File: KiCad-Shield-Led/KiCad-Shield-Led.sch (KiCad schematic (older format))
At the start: 8 parts, among them P1 Power, P2 Analog, P3 Digital, P4 Digital, P5 CONN_01X01, P6 CONN_01X01, P7 CONN_01X01, P8 CONN_01X01

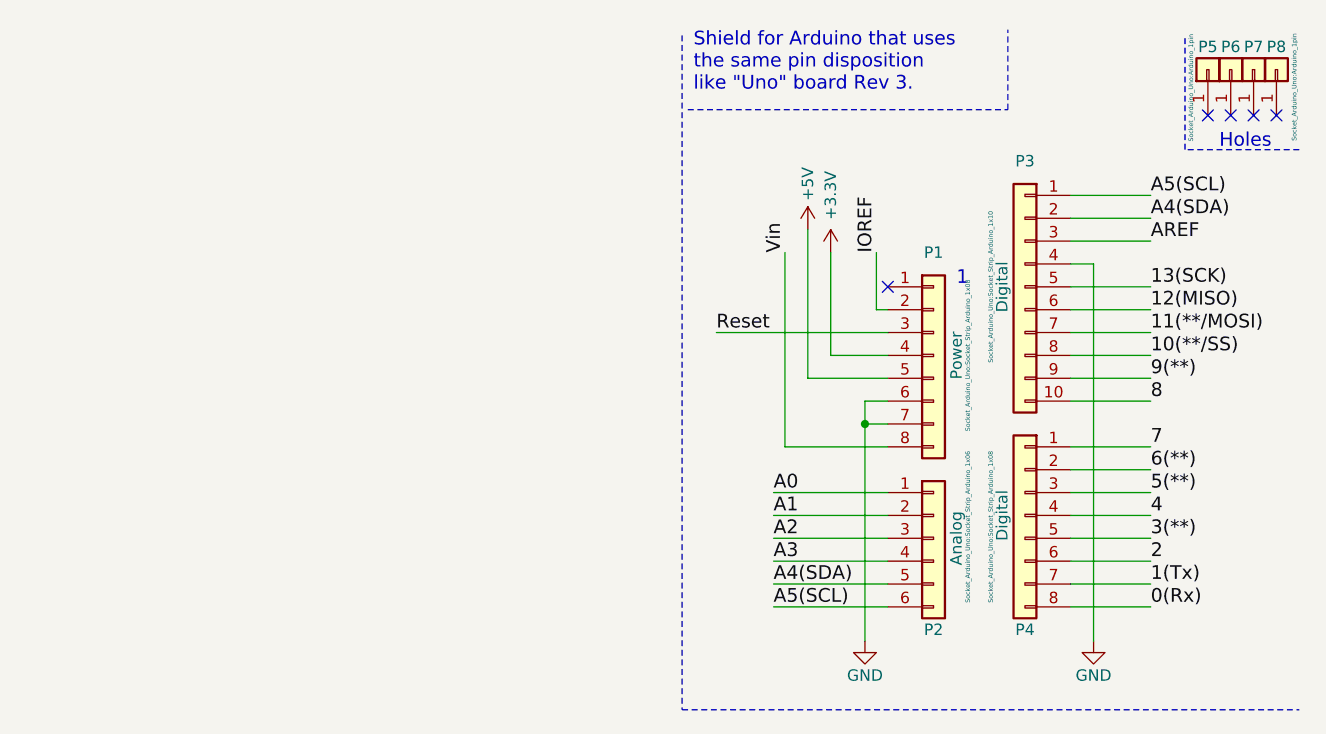
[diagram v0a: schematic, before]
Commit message: Dessin LED et R
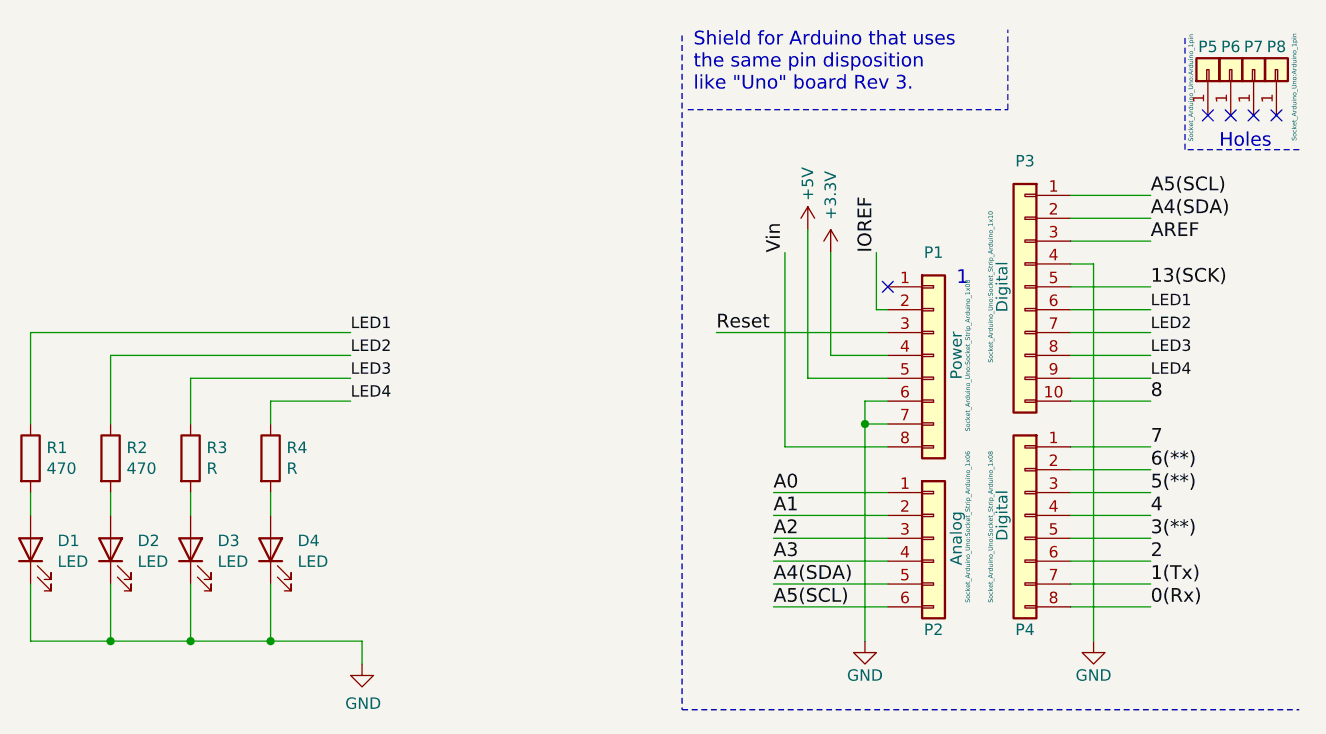
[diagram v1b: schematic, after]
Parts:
- added D1, D2, D3, D4: LED, symbol Device:LED
- added R1, R2: 470, symbol Device:R
- added R3, R4: R, symbol Device:R
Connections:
- net GND: now also D1.1 (K), D2.1 (K), D3.1 (K), D4.1 (K)
- net 10(**/SS) renamed LED3
- net LED3: now also R3.1
- net 11(**/MOSI) renamed LED2
- net LED2: now also R2.1
- net 12(MISO) renamed LED1
- net LED1: now also R1.1
- net 9(**) renamed LED4
- net LED4: now also R4.1
- new net: D1.2 (A), R1.2
- new net: D2.2 (A), R2.2
- new net: D3.2 (A), R3.2
- new net: D4.2 (A), R4.2
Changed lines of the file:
@@
 Text Label 10550 2100 0    60   ~ 0
 8
-Text Label 10550 2000 0    60   ~ 0
-9(**)
-Text Label 10550 1900 0    60   ~ 0
-10(**/SS)
-Text Label 10550 1800 0    60   ~ 0
-11(**/MOSI)
-Text Label 10550 1700 0    60   ~ 0
-12(MISO)
 Text Label 10550 1600 0    60   ~ 0
 13(SCK)
@@
 Wire Notes Line
 	10700 1000 10700 500
+$Comp
+L Device:LED D1
+U 1 1 5FC4CFF8
+P 5650 2750
+F 0 "D1" V 5689 2632 50  0000 R CNN
+F 1 "LED" V 5598 2632 50  0000 R CNN
+F 2 "" H 5650 2750 50  0001 C CNN
+F 3 "~" H 5650 2750 50  0001 C CNN
+	1    5650 2750
+	0    -1   -1   0
+$EndComp
+$Comp
+L Device:R R1
+U 1 1 5FC4E899
+P 5650 2350
+F 0 "R1" H 5720 2396 50  0000 L CNN
+F 1 "470" H 5720 2305 50  0000 L CNN
+F 2 "" V 5580 2350 50  0001 C CNN
+F 3 "~" H 5650 2350 50  0001 C CNN
+	1    5650 2350
+	1    0    0    -1
+$EndComp
+Wire Wire Line
+	5650 2500 5650 2600
+Wire Wire Line
+	5650 2900 5650 3150
+Wire Wire Line
+	5650 3150 6000 3150
+Wire Wire Line
+	7100 3150 7100 3250
+$Comp
+L Device:LED D2
+U 1 1 5FC5721B
+P 6000 2750
+F 0 "D2" V 6039 2632 50  0000 R CNN
+F 1 "LED" V 5948 2632 50  0000 R CNN
+F 2 "" H 6000 2750 50  0001 C CNN
+F 3 "~" H 6000 2750 50  0001 C CNN
+	1    6000 2750
+	0    -1   -1   0
+$EndComp
+$Comp
+L Device:R R2
+U 1 1 5FC5738B
+P 6000 2350
+F 0 "R2" H 6070 2396 50  0000 L CNN
+F 1 "470" H 6070 2305 50  0000 L CNN
+F 2 "" V 5930 2350 50  0001 C CNN
+F 3 "~" H 6000 2350 50  0001 C CNN
+	1    6000 2350
+	1    0    0    -1
+$EndComp
+Wire Wire Line
+	6000 2500 6000 2600
+Wire Wire Line
+	6000 2900 6000 3150
+Connection ~ 6000 3150
+Wire Wire Line
+	6000 3150 6350 3150
+$Comp
+L Device:LED D3
+U 1 1 5FC5A1AB
+P 6350 2750
+F 0 "D3" V 6389 2632 50  0000 R CNN
+F 1 "LED" V 6298 2632 50  0000 R CNN
+F 2 "" H 6350 2750 50  0001 C CNN
+F 3 "~" H 6350 2750 50  0001 C CNN
+	1    6350 2750
+	0    -1   -1   0
+$EndComp
+$Comp
+L Device:R R3
+U 1 1 5FC5A343
+P 6350 2350
+F 0 "R3" H 6420 2396 50  0000 L CNN
+F 1 "R" H 6420 2305 50  0000 L CNN
+F 2 "" V 6280 2350 50  0001 C CNN
+F 3 "~" H 6350 2350 50  0001 C CNN
+	1    6350 2350
+	1    0    0    -1
+$EndComp
+Wire Wire Line
+	6350 2500 6350 2600
+Wire Wire Line
+	6350 2900 6350 3150
+$Comp
+L Device:LED D4
+U 1 1 5FC5A34F
+P 6700 2750
+F 0 "D4" V 6739 2632 50  0000 R CNN
+F 1 "LED" V 6648 2632 50  0000 R CNN
+F 2 "" H 6700 2750 50  0001 C CNN
+F 3 "~" H 6700 2750 50  0001 C CNN
+	1    6700 2750
+	0    -1   -1   0
+$EndComp
+$Comp
+L Device:R R4
+U 1 1 5FC5A359
+P 6700 2350
+F 0 "R4" H 6770 2396 50  0000 L CNN
+F 1 "R" H 6770 2305 50  0000 L CNN
+F 2 "" V 6630 2350 50  0001 C CNN
+F 3 "~" H 6700 2350 50  0001 C CNN
+	1    6700 2350
+	1    0    0    -1
+$EndComp
+Wire Wire Line
+	6700 2500 6700 2600
+Wire Wire Line
+	6700 2900 6700 3150
+Connection ~ 6350 3150
+Wire Wire Line
+	6350 3150 6700 3150
+Connection ~ 6700 3150
+Wire Wire Line
+	6700 3150 7100 3150
+$Comp
+L power:GND #PWR05
+U 1 1 5FC5CA17
+P 7100 3250
+F 0 "#PWR05" H 7100 3000 50  0001 C CNN
+F 1 "GND" H 7105 3077 50  0000 C CNN
+F 2 "" H 7100 3250 50  0001 C CNN
+F 3 "" H 7100 3250 50  0001 C CNN
+	1    7100 3250
+	1    0    0    -1
+$EndComp
+Wire Wire Line
+	6700 2200 6700 2100
+Wire Wire Line
+	6700 2100 7050 2100
+Wire Wire Line
+	6350 2200 6350 2000
+Wire Wire Line
+	6350 2000 7050 2000
+Wire Wire Line
+	6000 1900 7050 1900
+Wire Wire Line
+	6000 1900 6000 2200
+Wire Wire Line
+	5650 2200 5650 1800
+Wire Wire Line
+	5650 1800 7050 1800
+Text Label 7050 1800 0    50   ~ 0
+LED1
+Text Label 7050 1900 0    50   ~ 0
+LED2
+Text Label 7050 2000 0    50   ~ 0
+LED3
+Text Label 7050 2100 0    50   ~ 0
+LED4
+Text Label 10550 1700 0    50   ~ 0
+LED1
+Text Label 10550 1800 0    50   ~ 0
+LED2
+Text Label 10550 1900 0    50   ~ 0
+LED3
+Text Label 10550 2000 0    50   ~ 0
+LED4
 $EndSCHEMATC

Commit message: Fin du shematique
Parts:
- R3, R4: value R -> 470
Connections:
- no-connect marks 5 -> 23
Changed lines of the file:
@@
 P 6350 2350
 F 0 "R3" H 6420 2396 50  0000 L CNN
-F 1 "R" H 6420 2305 50  0000 L CNN
+F 1 "470" H 6420 2305 50  0000 L CNN
 F 2 "" V 6280 2350 50  0001 C CNN
 F 3 "~" H 6350 2350 50  0001 C CNN
@@
 P 6700 2350
 F 0 "R4" H 6770 2396 50  0000 L CNN
-F 1 "R" H 6770 2305 50  0000 L CNN
+F 1 "470" H 6770 2305 50  0000 L CNN
 F 2 "" V 6630 2350 50  0001 C CNN
 F 3 "~" H 6700 2350 50  0001 C CNN
@@
 Text Label 10550 2000 0    50   ~ 0
 LED4
+NoConn ~ 8900 2500
+NoConn ~ 8900 2600
+NoConn ~ 8900 2700
+NoConn ~ 8900 2800
+NoConn ~ 10550 2300
+NoConn ~ 10550 2400
+NoConn ~ 10550 2500
+NoConn ~ 10550 2600
+NoConn ~ 10550 2700
+NoConn ~ 10550 2800
+NoConn ~ 10550 2900
+NoConn ~ 10550 3000
+NoConn ~ 10550 2100
+NoConn ~ 10550 1600
+NoConn ~ 10550 1400
+NoConn ~ 8950 1450
+NoConn ~ 9350 1450
+NoConn ~ 8650 1800
+$Comp
+L power:PWR_FLAG #FLG0101
+U 1 1 5FC89307
+P 7150 850
+F 0 "#FLG0101" H 7150 925 50  0001 C CNN
+F 1 "PWR_FLAG" H 7150 1023 50  0000 C CNN
+F 2 "" H 7150 850 50  0001 C CNN
+F 3 "~" H 7150 850 50  0001 C CNN
+	1    7150 850
+	1    0    0    -1
+$EndComp
+$Comp
+L power:GND #PWR0101
+U 1 1 5FC89CAC
+P 7150 850
+F 0 "#PWR0101" H 7150 600 50  0001 C CNN
+F 1 "GND" H 7150 700 50  0000 C CNN
+F 2 "" H 7150 850 50  0000 C CNN
+F 3 "" H 7150 850 50  0000 C CNN
+	1    7150 850
+	1    0    0    -1
+$EndComp
+$Comp
+L power:+3.3V #PWR0102
+U 1 1 5FC8AE1D
+P 7600 850
+F 0 "#PWR0102" H 7600 700 50  0001 C CNN
+F 1 "+3.3V" V 7600 1100 50  0000 C CNN
+F 2 "" H 7600 850 50  0000 C CNN
+F 3 "" H 7600 850 50  0000 C CNN
+	1    7600 850
+	-1   0    0    1
+$EndComp
+$Comp
+L power:+5V #PWR0103
+U 1 1 5FC8C4A5
+P 8050 850
+F 0 "#PWR0103" H 8050 700 50  0001 C CNN
+F 1 "+5V" V 8050 1050 50  0000 C CNN
+F 2 "" H 8050 850 50  0000 C CNN
+F 3 "" H 8050 850 50  0000 C CNN
+	1    8050 850
+	-1   0    0    1
+$EndComp
+$Comp
+L power:PWR_FLAG #FLG0102
+U 1 1 5FC917B8
+P 7600 850
+F 0 "#FLG0102" H 7600 925 50  0001 C CNN
+F 1 "PWR_FLAG" H 7600 1023 50  0000 C CNN
+F 2 "" H 7600 850 50  0001 C CNN
+F 3 "~" H 7600 850 50  0001 C CNN
+	1    7600 850
+	1    0    0    -1
+$EndComp
+$Comp
+L power:PWR_FLAG #FLG0103
+U 1 1 5FC91CC0
+P 8050 850
+F 0 "#FLG0103" H 8050 925 50  0001 C CNN
+F 1 "PWR_FLAG" H 8050 1023 50  0000 C CNN
+F 2 "" H 8050 850 50  0001 C CNN
+F 3 "~" H 8050 850 50  0001 C CNN
+	1    8050 850
+	1    0    0    -1
+$EndComp
 $EndSCHEMATC

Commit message: Generation de la Netlist
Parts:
- D1, D2, D3, D4: footprint (none) -> LED_THT:LED_D5.0mm
- R1, R2, R3, R4: footprint (none) -> Resistor_THT:R_Axial_DIN0207_L6.3mm_D2.5mm_P10.16mm_Horizontal
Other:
- moved on the sheet: D1, D2, D3, D4, R1, R2, R3, R4
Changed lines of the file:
@@
 L Device:LED D1
 U 1 1 5FC4CFF8
-P 5650 2750
-F 0 "D1" V 5689 2632 50  0000 R CNN
-F 1 "LED" V 5598 2632 50  0000 R CNN
-F 2 "" H 5650 2750 50  0001 C CNN
-F 3 "~" H 5650 2750 50  0001 C CNN
-	1    5650 2750
+P 6300 2750
+F 0 "D1" V 6339 2632 50  0000 R CNN
+F 1 "LED" V 6248 2632 50  0000 R CNN
+F 2 "LED_THT:LED_D5.0mm" H 6300 2750 50  0001 C CNN
+F 3 "~" H 6300 2750 50  0001 C CNN
+	1    6300 2750
 	0    -1   -1   0
 $EndComp
@@
 L Device:R R1
 U 1 1 5FC4E899
-P 5650 2350
-F 0 "R1" H 5720 2396 50  0000 L CNN
-F 1 "470" H 5720 2305 50  0000 L CNN
-F 2 "" V 5580 2350 50  0001 C CNN
-F 3 "~" H 5650 2350 50  0001 C CNN
-	1    5650 2350
+P 6300 2350
+F 0 "R1" H 6370 2396 50  0000 L CNN
+F 1 "470" H 6370 2305 50  0000 L CNN
+F 2 "Resistor_THT:R_Axial_DIN0207_L6.3mm_D2.5mm_P10.16mm_Horizontal" V 6230 2350 50  0001 C CNN
+F 3 "~" H 6300 2350 50  0001 C CNN
+	1    6300 2350
 	1    0    0    -1
 $EndComp
 Wire Wire Line
-	5650 2500 5650 2600
+	6300 2500 6300 2600
 Wire Wire Line
-	5650 2900 5650 3150
+	6300 2900 6300 3150
 Wire Wire Line
-	5650 3150 6000 3150
+	6300 3150 6650 3150
 Wire Wire Line
-	7100 3150 7100 3250
+	7750 3150 7750 3250
 $Comp
 L Device:LED D2
 U 1 1 5FC5721B
-P 6000 2750
-F 0 "D2" V 6039 2632 50  0000 R CNN
-F 1 "LED" V 5948 2632 50  0000 R CNN
-F 2 "" H 6000 2750 50  0001 C CNN
-F 3 "~" H 6000 2750 50  0001 C CNN
-	1    6000 2750
+P 6650 2750
+F 0 "D2" V 6689 2632 50  0000 R CNN
+F 1 "LED" V 6598 2632 50  0000 R CNN
+F 2 "LED_THT:LED_D5.0mm" H 6650 2750 50  0001 C CNN
+F 3 "~" H 6650 2750 50  0001 C CNN
+	1    6650 2750
 	0    -1   -1   0
 $EndComp
@@
 L Device:R R2
 U 1 1 5FC5738B
-P 6000 2350
-F 0 "R2" H 6070 2396 50  0000 L CNN
-F 1 "470" H 6070 2305 50  0000 L CNN
-F 2 "" V 5930 2350 50  0001 C CNN
-F 3 "~" H 6000 2350 50  0001 C CNN
-	1    6000 2350
+P 6650 2350
+F 0 "R2" H 6720 2396 50  0000 L CNN
+F 1 "470" H 6720 2305 50  0000 L CNN
+F 2 "Resistor_THT:R_Axial_DIN0207_L6.3mm_D2.5mm_P10.16mm_Horizontal" V 6580 2350 50  0001 C CNN
+F 3 "~" H 6650 2350 50  0001 C CNN
+	1    6650 2350
 	1    0    0    -1
 $EndComp
 Wire Wire Line
-	6000 2500 6000 2600
+	6650 2500 6650 2600
 Wire Wire Line
-	6000 2900 6000 3150
-Connection ~ 6000 3150
+	6650 2900 6650 3150
+Connection ~ 6650 3150
 Wire Wire Line
-	6000 3150 6350 3150
+	6650 3150 7000 3150
 $Comp
 L Device:LED D3
 U 1 1 5FC5A1AB
-P 6350 2750
-F 0 "D3" V 6389 2632 50  0000 R CNN
-F 1 "LED" V 6298 2632 50  0000 R CNN
-F 2 "" H 6350 2750 50  0001 C CNN
-F 3 "~" H 6350 2750 50  0001 C CNN
-	1    6350 2750
+P 7000 2750
+F 0 "D3" V 7039 2632 50  0000 R CNN
+F 1 "LED" V 6948 2632 50  0000 R CNN
+F 2 "LED_THT:LED_D5.0mm" H 7000 2750 50  0001 C CNN
+F 3 "~" H 7000 2750 50  0001 C CNN
+	1    7000 2750
 	0    -1   -1   0
 $EndComp
@@
 L Device:R R3
 U 1 1 5FC5A343
-P 6350 2350
-F 0 "R3" H 6420 2396 50  0000 L CNN
-F 1 "470" H 6420 2305 50  0000 L CNN
-F 2 "" V 6280 2350 50  0001 C CNN
-F 3 "~" H 6350 2350 50  0001 C CNN
-	1    6350 2350
+P 7000 2350
+F 0 "R3" H 7070 2396 50  0000 L CNN
+F 1 "470" H 7070 2305 50  0000 L CNN
+F 2 "Resistor_THT:R_Axial_DIN0207_L6.3mm_D2.5mm_P10.16mm_Horizontal" V 6930 2350 50  0001 C CNN
+F 3 "~" H 7000 2350 50  0001 C CNN
+	1    7000 2350
 	1    0    0    -1
 $EndComp
 Wire Wire Line
-	6350 2500 6350 2600
+	7000 2500 7000 2600
 Wire Wire Line
-	6350 2900 6350 3150
+	7000 2900 7000 3150
 $Comp
 L Device:LED D4
 U 1 1 5FC5A34F
-P 6700 2750
-F 0 "D4" V 6739 2632 50  0000 R CNN
-F 1 "LED" V 6648 2632 50  0000 R CNN
-F 2 "" H 6700 2750 50  0001 C CNN
-F 3 "~" H 6700 2750 50  0001 C CNN
-	1    6700 2750
+P 7350 2750
+F 0 "D4" V 7389 2632 50  0000 R CNN
+F 1 "LED" V 7298 2632 50  0000 R CNN
+F 2 "LED_THT:LED_D5.0mm" H 7350 2750 50  0001 C CNN
+F 3 "~" H 7350 2750 50  0001 C CNN
+	1    7350 2750
 	0    -1   -1   0
 $EndComp
@@
 L Device:R R4
 U 1 1 5FC5A359
-P 6700 2350
-F 0 "R4" H 6770 2396 50  0000 L CNN
-F 1 "470" H 6770 2305 50  0000 L CNN
-F 2 "" V 6630 2350 50  0001 C CNN
-F 3 "~" H 6700 2350 50  0001 C CNN
-	1    6700 2350
+P 7350 2350
+F 0 "R4" H 7420 2396 50  0000 L CNN
+F 1 "470" H 7420 2305 50  0000 L CNN
+F 2 "Resistor_THT:R_Axial_DIN0207_L6.3mm_D2.5mm_P10.16mm_Horizontal" V 7280 2350 50  0001 C CNN
+F 3 "~" H 7350 2350 50  0001 C CNN
+	1    7350 2350
 	1    0    0    -1
 $EndComp
 Wire Wire Line
-	6700 2500 6700 2600
+	7350 2500 7350 2600
 Wire Wire Line
-	6700 2900 6700 3150
-Connection ~ 6350 3150
+	7350 2900 7350 3150
+Connection ~ 7000 3150
 Wire Wire Line
-	6350 3150 6700 3150
-Connection ~ 6700 3150
+	7000 3150 7350 3150
+Connection ~ 7350 3150
 Wire Wire Line
-	6700 3150 7100 3150
+	7350 3150 7750 3150
 $Comp
 L power:GND #PWR05
 U 1 1 5FC5CA17
-P 7100 3250
-F 0 "#PWR05" H 7100 3000 50  0001 C CNN
-F 1 "GND" H 7105 3077 50  0000 C CNN
-F 2 "" H 7100 3250 50  0001 C CNN
-F 3 "" H 7100 3250 50  0001 C CNN
-	1    7100 3250
+P 7750 3250
+F 0 "#PWR05" H 7750 3000 50  0001 C CNN
+F 1 "GND" H 7755 3077 50  0000 C CNN
+F 2 "" H 7750 3250 50  0001 C CNN
+F 3 "" H 7750 3250 50  0001 C CNN
+	1    7750 3250
 	1    0    0    -1
 $EndComp
 Wire Wire Line
-	6700 2200 6700 2100
+	7350 2200 7350 2100
 Wire Wire Line
-	6700 2100 7050 2100
+	7350 2100 7700 2100
 Wire Wire Line
-	6350 2200 6350 2000
+	7000 2200 7000 2000
 Wire Wire Line
-	6350 2000 7050 2000
+	7000 2000 7700 2000
 Wire Wire Line
-	6000 1900 7050 1900
+	6650 1900 7700 1900
 Wire Wire Line
-	6000 1900 6000 2200
+	6650 1900 6650 2200
 Wire Wire Line
-	5650 2200 5650 1800
+	6300 2200 6300 1800
 Wire Wire Line
-	5650 1800 7050 1800
-Text Label 7050 1800 0    50   ~ 0
+	6300 1800 7700 1800
+Text Label 7700 1800 0    50   ~ 0
 LED1
-Text Label 7050 1900 0    50   ~ 0
+Text Label 7700 1900 0    50   ~ 0
 LED2
-Text Label 7050 2000 0    50   ~ 0
+Text Label 7700 2000 0    50   ~ 0
 LED3
-Text Label 7050 2100 0    50   ~ 0
+Text Label 7700 2100 0    50   ~ 0
 LED4
 Text Label 10550 1700 0    50   ~ 0
